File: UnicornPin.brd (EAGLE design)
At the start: 61.4 x 52.1 mm, 8 parts

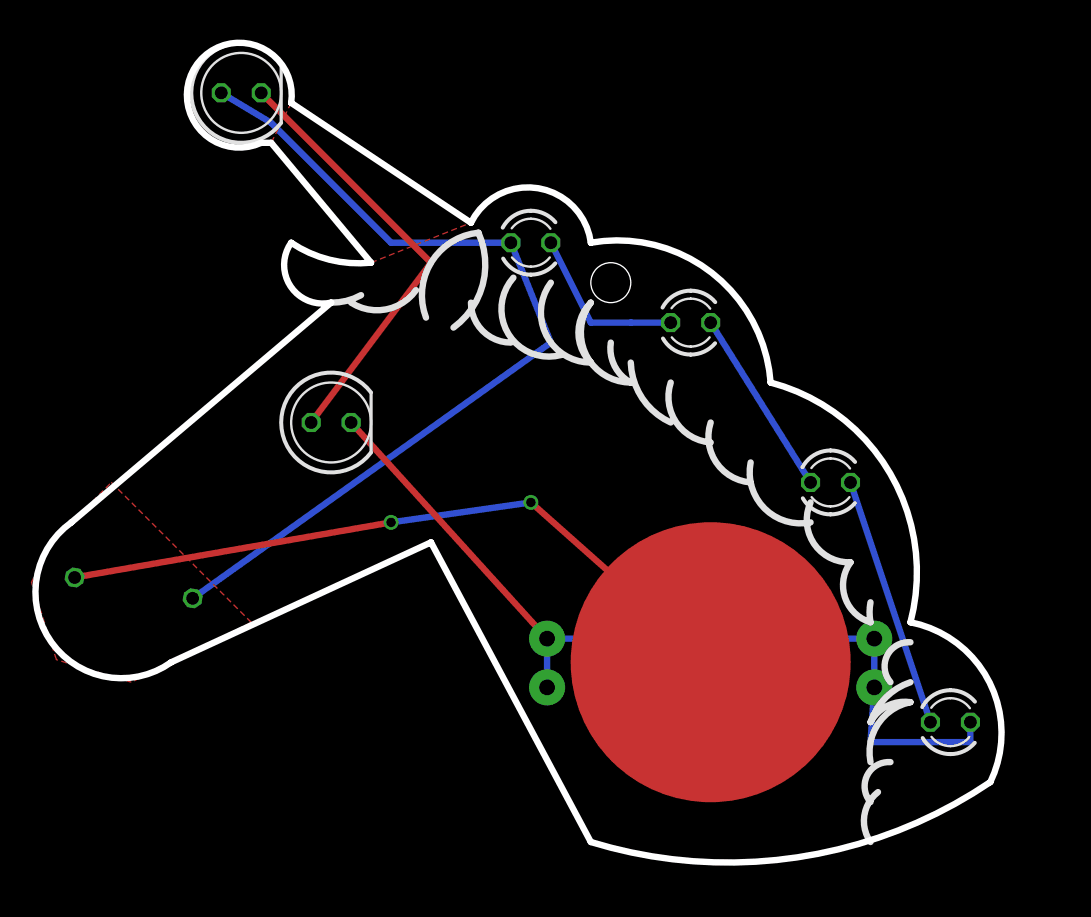
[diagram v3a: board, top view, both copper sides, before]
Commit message: routed unicorn board to fit the new schematic
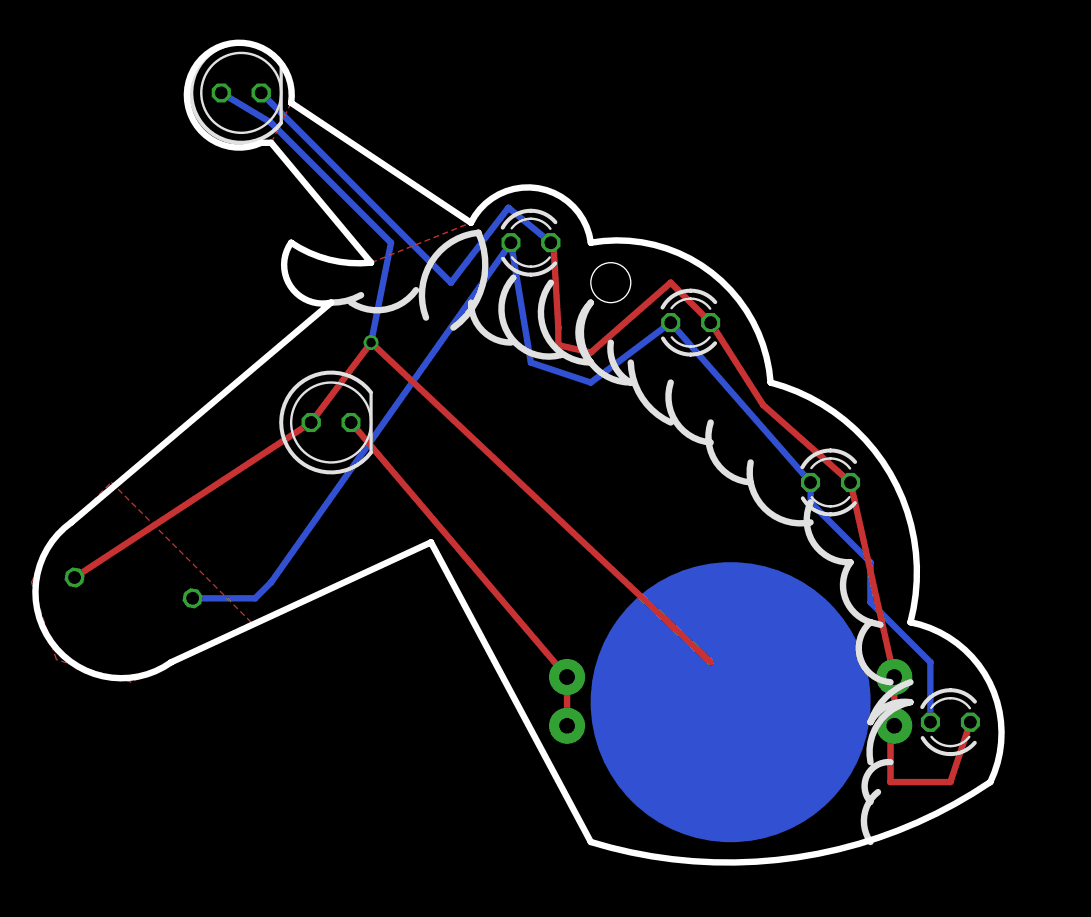
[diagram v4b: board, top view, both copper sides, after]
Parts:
- moved U$1 2.84 mm to (57.1, 35.6), flipped to the bottom, turned to 180 degrees
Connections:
- removed net N$4: LED3.K, LED4.A
- removed net N$5: LED4.K, LED5.A
- removed net N$6: LED1.A, LED6.K
- removed net N$7: R1.1, U$1.P$5
- net N$1: now also LED1.A, R1.1, U$1.P$5; no longer LED2.A, R1.2
- net N$2: now also LED2.K, LED3.K, LED4.K, LED6.K
- net N$3: now also LED2.A, LED4.A, LED5.A, R1.2; no longer LED2.K
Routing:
- net N$3: track 10.8 -> 81.8 mm
- net N$2: track 56.7 -> 111.0 mm
- net N$7: track 44.7 -> 0.00 mm, vias 2 -> 0
- net N$6: track 28.0 -> 0.00 mm
- net N$1: track 56.9 -> 74.9 mm, vias 0 -> 1
- net N$5: track 16.1 -> 0.00 mm
- net N$4: track 12.0 -> 0.00 mm
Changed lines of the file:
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@@
 <grid distance="0.05" unitdist="inch" unit="inch" style="lines" multiple="1" display="no" altdistance="0.00625" altunitdist="inch" altunit="inch"/>
 <layers>
-<layer number="1" name="Top" color="4" fill="1" visible="no" active="yes"/>
+<layer number="1" name="Top" color="4" fill="1" visible="yes" active="yes"/>
 <layer number="16" name="Bottom" color="1" fill="1" visible="yes" active="yes"/>
 <layer number="17" name="Pads" color="2" fill="1" visible="yes" active="yes"/>
@@
 <wire x1="62.23" y1="48.26" x2="64.77" y2="44.45" width="0.4064" layer="21" curve="116.565051"/>
 <wire x1="64.77" y1="44.45" x2="66.04" y2="40.64" width="0.4064" layer="21" curve="109.653824"/>
-<wire x1="68.58" y1="39.37" x2="67.31" y2="36.83" width="0.4064" layer="21" curve="135"/>
+<wire x1="66.04" y1="40.64" x2="67.31" y2="36.83" width="0.4064" layer="21" curve="135"/>
 <wire x1="68.58" y1="36.83" x2="66.04" y2="34.29" width="0.4064" layer="21" curve="53.130102"/>
 <wire x1="66.04" y1="34.29" x2="68.58" y2="35.56" width="0.4064" layer="21" curve="-70.346176"/>
@@
 <wire x1="33.02" y1="60.96" x2="37.1475" y2="61.75375" width="0.4064" layer="21" curve="87.49686"/>
 <wire x1="40.64" y1="60.96" x2="43.18" y2="58.42" width="0.4064" layer="21" curve="90"/>
-<wire x1="66.04" y1="40.64" x2="66.04" y2="41.91" width="0.4064" layer="21" curve="-21.801409"/>
 <wire x1="66.04" y1="29.21" x2="67.31" y2="31.75" width="0.4064" layer="21" curve="-135"/>
 <wire x1="66.04" y1="26.67" x2="66.51625" y2="29.845" width="0.4064" layer="21" curve="-86.82017"/>
+<wire x1="66.04" y1="40.64" x2="66.675" y2="40.48125" width="0.4064" layer="21"/>
 </plain>
 <attributes>
@@
 <attribute name="VALUE" x="73.025" y="32.639" size="1.27" layer="27" ratio="10"/>
 </element>
-<element name="U$1" library="battery" package="BAT-HLD-001-THM" value="CR2032-GK" x="55.88" y="38.1"/>
+<element name="U$1" library="battery" package="BAT-HLD-001-THM" value="CR2032-GK" x="57.15" y="35.56" rot="MR180"/>
 <element name="LED6" library="led" package="LED5MM" value="" x="26.035" y="74.295" smashed="yes">
 <attribute name="NAME" x="27.94" y="72.2884" size="1.27" layer="26" ratio="10" rot="MR0"/>
@@
 </elements>
 <signals>
-<signal name="N$1">
-<contactref element="LED2" pad="A"/>
-<contactref element="LED6" pad="A"/>
-<contactref element="R1" pad="2"/>
-<wire x1="22.947321875" y1="42.162965625" x2="45.72" y2="58.42" width="0.4064" layer="16"/>
-<wire x1="45.72" y1="58.42" x2="43.18" y2="64.77" width="0.4064" layer="16"/>
-<wire x1="43.18" y1="64.77" x2="35.56" y2="64.77" width="0.4064" layer="16"/>
-<wire x1="24.765" y1="74.295" x2="27.94" y2="72.39" width="0.4064" layer="16"/>
-<wire x1="27.94" y1="72.39" x2="35.56" y2="64.77" width="0.4064" layer="16"/>
-</signal>
-<signal name="N$2">
-<contactref element="U$1" pad="P$1"/>
-<contactref element="U$1" pad="P$2"/>
-<contactref element="U$1" pad="P$3"/>
-<contactref element="U$1" pad="P$4"/>
-<contactref element="LED1" pad="K"/>
-<contactref element="LED5" pad="K"/>
-<wire x1="66.28" y1="36.5" x2="66.28" y2="39.6" width="0.4064" layer="16"/>
-<wire x1="66.28" y1="39.6" x2="45.48" y2="39.6" width="0.4064" layer="16"/>
-<wire x1="45.48" y1="39.6" x2="33.02" y2="53.34" width="0.4064" layer="1"/>
-<wire x1="45.48" y1="36.5" x2="45.48" y2="39.6" width="0.4064" layer="16"/>
-<wire x1="66.28" y1="36.5" x2="66.04" y2="33.02" width="0.4064" layer="16"/>
-<wire x1="66.04" y1="33.02" x2="72.39" y2="33.02" width="0.4064" layer="16"/>
-<wire x1="72.39" y1="33.02" x2="72.39" y2="34.29" width="0.4064" layer="16"/>
-</signal>
-<signal name="N$3">
-<contactref element="LED2" pad="K"/>
-<contactref element="LED3" pad="A"/>
-<wire x1="45.72" y1="64.77" x2="48.26" y2="59.69" width="0.4064" layer="16"/>
-<wire x1="48.26" y1="59.69" x2="50.8" y2="59.69" width="0.4064" layer="16"/>
-<wire x1="50.8" y1="59.69" x2="53.34" y2="59.69" width="0.4064" layer="16"/>
-</signal>
-<signal name="N$4">
-<contactref element="LED3" pad="K"/>
-<contactref element="LED4" pad="A"/>
-<wire x1="55.88" y1="59.69" x2="62.23" y2="49.53" width="0.4064" layer="16"/>
-</signal>
-<signal name="N$5">
-<contactref element="LED4" pad="K"/>
-<contactref element="LED5" pad="A"/>
-<wire x1="64.77" y1="49.53" x2="67.31" y2="41.91" width="0" layer="19" extent="1-16"/>
-<wire x1="64.77" y1="49.53" x2="69.85" y2="34.29" width="0.4064" layer="16"/>
-<wire x1="67.31" y1="40.64" x2="67.31" y2="41.91" width="0" layer="19" curve="-180" extent="1-16"/>
-</signal>
 <signal name="N$6">
-<contactref element="LED1" pad="A"/>
-<contactref element="LED6" pad="K"/>
-<wire x1="27.305" y1="74.295" x2="38.1" y2="63.5" width="0.4064" layer="1"/>
-<wire x1="38.1" y1="63.5" x2="30.48" y2="53.34" width="0.4064" layer="1"/>
 <polygon width="0.4064" layer="1" orphans="yes">
 <vertex x="34.29" y="63.5"/>
@@
 </signal>
 <signal name="N$7">
-<contactref element="U$1" pad="P$5"/>
-<contactref element="R1" pad="1"/>
-<wire x1="15.4430875" y1="43.4861625" x2="35.56" y2="46.99" width="0.4064" layer="1"/>
-<via x="35.56" y="46.99" extent="1-16" drill="0.6" shape="square"/>
-<wire x1="35.56" y1="46.99" x2="44.45" y2="48.26" width="0.4064" layer="16"/>
-<via x="44.45" y="48.26" extent="1-16" drill="0.6" shape="square"/>
-<wire x1="44.45" y1="48.26" x2="55.88" y2="38.1" width="0.4064" layer="1"/>
 <polygon width="0.4064" layer="1" orphans="yes">
 <vertex x="17.78" y="49.53"/>
@@
 </polygon>
 </signal>
+<signal name="N$1">
+<contactref element="U$1" pad="P$5"/>
+<contactref element="LED1" pad="A"/>
+<contactref element="LED6" pad="A"/>
+<contactref element="R1" pad="1"/>
+<wire x1="30.48" y1="53.34" x2="15.4430875" y2="43.4861625" width="0.4064" layer="1"/>
+<wire x1="30.48" y1="53.34" x2="34.29" y2="58.42" width="0.4064" layer="1"/>
+<wire x1="34.29" y1="58.42" x2="55.88" y2="38.1" width="0.4064" layer="1"/>
+<via x="34.29" y="58.42" extent="1-16" drill="0.6" shape="square"/>
+<wire x1="34.29" y1="58.42" x2="35.56" y2="64.77" width="0.4064" layer="16"/>
+<wire x1="35.56" y1="64.77" x2="27.94" y2="72.39" width="0.4064" layer="16"/>
+<wire x1="27.94" y1="72.39" x2="24.765" y2="74.295" width="0.4064" layer="16"/>
+<wire x1="55.88" y1="38.1" x2="57.15" y2="35.56" width="0" layer="19" extent="1-16"/>
+</signal>
+<signal name="N$2">
+<contactref element="U$1" pad="P$3"/>
+<contactref element="U$1" pad="P$1"/>
+<contactref element="U$1" pad="P$2"/>
+<contactref element="U$1" pad="P$4"/>
+<contactref element="LED1" pad="K"/>
+<contactref element="LED6" pad="K"/>
+<contactref element="LED2" pad="K"/>
+<contactref element="LED3" pad="K"/>
+<contactref element="LED4" pad="K"/>
+<contactref element="LED5" pad="K"/>
+<wire x1="45.72" y1="64.77" x2="45.87875" y2="64.77" width="0.4064" layer="1"/>
+<wire x1="45.87875" y1="64.77" x2="46.19625" y2="59.3725" width="0.4064" layer="1"/>
+<wire x1="46.19625" y1="59.3725" x2="46.19625" y2="58.26125" width="0.4064" layer="1"/>
+<wire x1="46.19625" y1="58.26125" x2="48.26" y2="57.785" width="0.4064" layer="1"/>
+<wire x1="48.26" y1="57.785" x2="53.34" y2="62.23" width="0.4064" layer="1"/>
+<wire x1="53.34" y1="62.23" x2="55.88" y2="59.69" width="0.4064" layer="1"/>
+<wire x1="64.77" y1="49.53" x2="67.55" y2="37.16" width="0.4064" layer="1"/>
+<wire x1="67.55" y1="37.16" x2="67.55" y2="34.06" width="0.4064" layer="1"/>
+<wire x1="67.55" y1="34.06" x2="67.69875" y2="33.7425" width="0.4064" layer="1"/>
+<wire x1="33.02" y1="53.34" x2="46.75" y2="37.16" width="0.4064" layer="1"/>
+<wire x1="46.75" y1="37.16" x2="46.75" y2="34.06" width="0.4064" layer="1"/>
+<wire x1="55.88" y1="59.69" x2="59.21375" y2="54.45125" width="0.4064" layer="1"/>
+<wire x1="59.21375" y1="54.45125" x2="64.77" y2="49.53" width="0.4064" layer="1"/>
+<wire x1="67.69875" y1="33.7425" x2="67.31" y2="33.35375" width="0.4064" layer="1"/>
+<wire x1="67.31" y1="33.35375" x2="67.31" y2="30.48" width="0.4064" layer="1"/>
+<wire x1="67.31" y1="30.48" x2="71.12" y2="30.48" width="0.4064" layer="1"/>
+<wire x1="71.12" y1="30.48" x2="72.39" y2="34.29" width="0.4064" layer="1"/>
+<wire x1="27.305" y1="74.295" x2="39.37" y2="62.23" width="0.4064" layer="16"/>
+<wire x1="39.37" y1="62.23" x2="43.02125" y2="66.9925" width="0.4064" layer="16"/>
+<wire x1="43.02125" y1="66.9925" x2="45.72" y2="64.77" width="0.4064" layer="16"/>
+<wire x1="33.02" y1="53.34" x2="39.37" y2="62.23" width="0" layer="19" extent="16-16"/>
+</signal>
+<signal name="N$3">
+<contactref element="LED5" pad="A"/>
+<contactref element="LED2" pad="A"/>
+<contactref element="R1" pad="2"/>
+<contactref element="LED3" pad="A"/>
+<contactref element="LED4" pad="A"/>
+<wire x1="22.947321875" y1="42.162965625" x2="26.922965625" y2="42.162965625" width="0.4064" layer="16"/>
+<wire x1="26.922965625" y1="42.162965625" x2="27.94" y2="43.18" width="0.4064" layer="16"/>
+<wire x1="27.94" y1="43.18" x2="43.18" y2="64.77" width="0.4064" layer="16"/>
+<wire x1="43.18" y1="64.77" x2="44.45" y2="57.15" width="0.4064" layer="16"/>
+<wire x1="44.45" y1="57.15" x2="48.26" y2="55.88" width="0.4064" layer="16"/>
+<wire x1="48.26" y1="55.88" x2="53.34" y2="59.69" width="0.4064" layer="16"/>
+<wire x1="53.34" y1="59.69" x2="62.23" y2="49.53" width="0.4064" layer="16"/>
+<wire x1="62.23" y1="49.53" x2="62.23" y2="48.26" width="0.4064" layer="16"/>
+<wire x1="62.23" y1="48.26" x2="66.04" y2="44.45" width="0.4064" layer="16"/>
+<wire x1="66.04" y1="44.45" x2="66.04" y2="41.91" width="0.4064" layer="16"/>
+<wire x1="66.04" y1="41.91" x2="69.85" y2="38.1" width="0.4064" layer="16"/>
+<wire x1="69.85" y1="38.1" x2="69.85" y2="34.29" width="0.4064" layer="16"/>
+</signal>
 </signals>
